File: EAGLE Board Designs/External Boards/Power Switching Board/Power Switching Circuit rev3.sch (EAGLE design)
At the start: 65 parts, among them J1 CONNECTOR-3_, J2 CONNECTOR-4_SOURIAU_, J3 CONNECTOR-4_SOURIAU_, Q1 TRANSISTOR_N_MOS_2-7K1S_TK100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, Q2 TRANSISTOR_N_MOS_2-7K1S_TK100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, Q3 TRANSISTOR_N_MOS_2-7K1S_TK100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, Q4 TRANSISTOR_N_MOS_2-7K1S_TK100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, U1 LTC4421

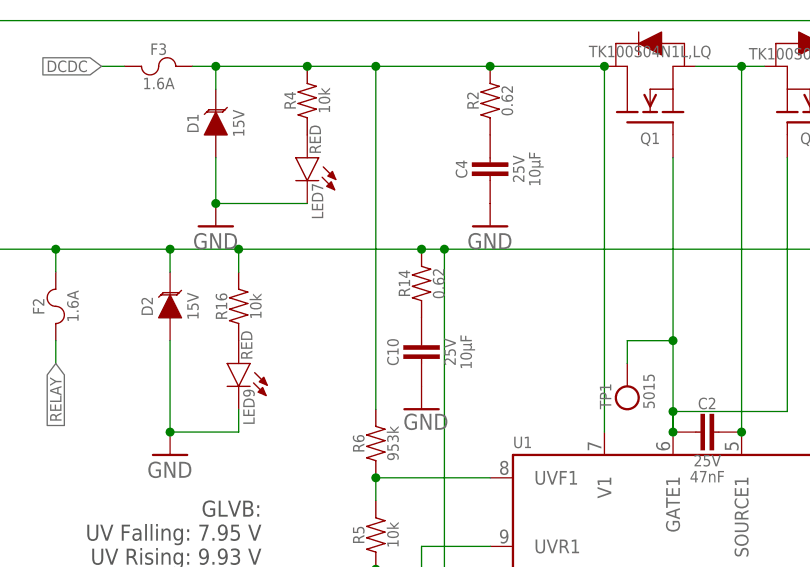
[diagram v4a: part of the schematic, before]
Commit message: Replaced 0.62 resistors with one in library
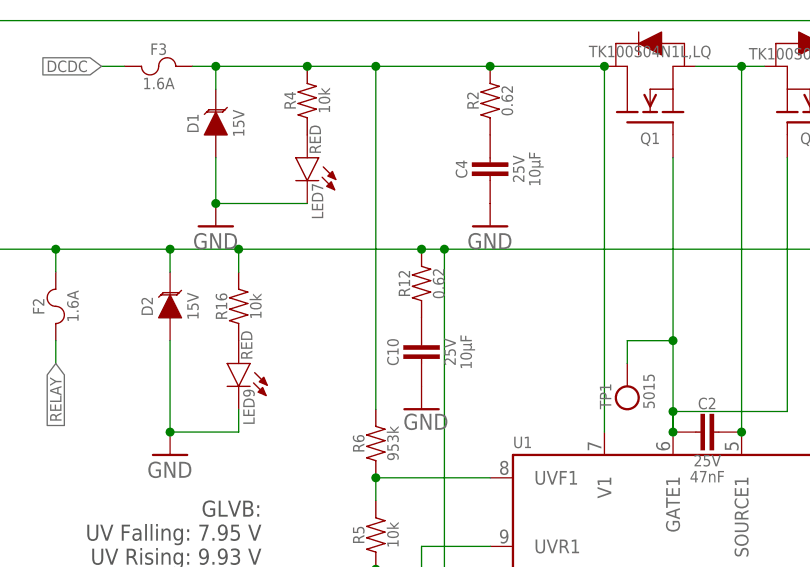
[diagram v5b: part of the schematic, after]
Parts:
- removed R14: 0.62, HyTechDevices:RESISTOR0805
- added R12: RESISTOR_0805_0.62, HyTechDevices:RESISTOR_0805_0.62
- R2: value 0.62 -> RESISTOR_0805_0.62; device HyTechDevices:RESISTOR0805 -> HyTechDevices:RESISTOR_0805_0.62
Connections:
- net N$4: now also R12.1; no longer R14.1
- net RELAY: now also R12.2; no longer R14.2
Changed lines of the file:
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@@
 <part name="GND10" library="HyTechSupplies" deviceset="GND" device=""/>
 <part name="GND11" library="HyTechSupplies" deviceset="GND" device=""/>
-<part name="R14" library="HyTechDevices" deviceset="RESISTOR" device="0805" value="0.62"/>
 <part name="GND12" library="HyTechSupplies" deviceset="GND" device=""/>
-<part name="R2" library="HyTechDevices" deviceset="RESISTOR" device="0805" value="0.62"/>
 <part name="GND13" library="HyTechSymbols" deviceset="GND" device=""/>
 <part name="D2" library="HyTechDevices" deviceset="TVS_*" device="" technology="15V"/>
@@
 <part name="GND15" library="HyTechSupplies" deviceset="GND" device=""/>
 <part name="C11" library="HyTechDevices" deviceset="CAPACITOR_?_*" device="0603" technology="25V_0.1UF"/>
+<part name="R2" library="HyTechDevices" deviceset="RESISTOR_?_*" device="0805" technology="0.62"/>
+<part name="R12" library="HyTechDevices" deviceset="RESISTOR_?_*" device="0805" technology="0.62"/>
 </parts>
 <sheets>
@@
 <attribute name="VALUE" x="-42.672" y="5.334" size="1.778" layer="96"/>
 </instance>
-<instance part="R14" gate="G$1" x="-40.64" y="22.86" smashed="yes" rot="R90">
-<attribute name="NAME" x="-41.91" y="21.59" size="1.27" layer="95" rot="R90" align="bottom-center"/>
-<attribute name="VALUE" x="-39.37" y="21.59" size="1.27" layer="96" rot="R90" align="top-center"/>
-</instance>
 <instance part="GND12" gate="1" x="-33.02" y="27.94" smashed="yes">
 <attribute name="VALUE" x="-35.56" y="25.4" size="1.778" layer="96"/>
-</instance>
-<instance part="R2" gate="G$1" x="-33.02" y="43.18" smashed="yes" rot="R90">
-<attribute name="NAME" x="-34.29" y="41.91" size="1.27" layer="95" rot="R90" align="bottom-center"/>
-<attribute name="VALUE" x="-31.75" y="41.91" size="1.27" layer="96" rot="R90" align="top-center"/>
 </instance>
 <instance part="GND13" gate="1" x="83.82" y="-30.48" smashed="yes">
@@
 <attribute name="VOLTAGE" x="40.64" y="87.63" size="1.27" layer="96" rot="R270" align="top-center"/>
 <attribute name="CAPACITANCE" x="38.862" y="87.63" size="1.27" layer="96" rot="R270" align="top-center"/>
+</instance>
+<instance part="R2" gate="G$1" x="-33.02" y="43.18" smashed="yes" rot="R90">
+<attribute name="NAME" x="-34.29" y="41.91" size="1.27" layer="95" rot="R90" align="bottom-center"/>
+<attribute name="RESISTANCE" x="-31.75" y="41.91" size="1.27" layer="96" rot="R90" align="top-center"/>
+</instance>
+<instance part="R12" gate="G$1" x="-40.64" y="22.86" smashed="yes" rot="R90">
+<attribute name="NAME" x="-41.91" y="21.59" size="1.27" layer="95" rot="R90" align="bottom-center"/>
+<attribute name="RESISTANCE" x="-39.37" y="21.59" size="1.27" layer="96" rot="R90" align="top-center"/>
 </instance>
 </instances>
@@
 <pinref part="U1" gate="G$1" pin="V1"/>
 <wire x1="-20.32" y1="5.08" x2="-20.32" y2="45.72" width="0.1524" layer="91"/>
+<junction x="-20.32" y="45.72"/>
+<pinref part="Q1" gate="G$1" pin="D"/>
 <wire x1="-20.32" y1="45.72" x2="-33.02" y2="45.72" width="0.1524" layer="91"/>
-<junction x="-20.32" y="45.72"/>
-<pinref part="R2" gate="G$1" pin="2"/>
-<pinref part="Q1" gate="G$1" pin="D"/>
+<pinref part="R4" gate="G$1" pin="2"/>
 <wire x1="-33.02" y1="45.72" x2="-45.72" y2="45.72" width="0.1524" layer="91"/>
-<junction x="-33.02" y="45.72"/>
-<pinref part="R4" gate="G$1" pin="2"/>
 <wire x1="-45.72" y1="45.72" x2="-53.34" y2="45.72" width="0.1524" layer="91"/>
 <wire x1="-53.34" y1="45.72" x2="-63.5" y2="45.72" width="0.1524" layer="91"/>
@@
 <junction x="-45.72" y="45.72"/>
 <pinref part="F3" gate="G$1" pin="2"/>
+<pinref part="R2" gate="G$1" pin="2"/>
+<junction x="-33.02" y="45.72"/>
 </segment>
 <segment>
@@
 <net name="RELAY" class="0">
 <segment>
-<pinref part="R14" gate="G$1" pin="2"/>
 <pinref part="R16" gate="G$1" pin="2"/>
 <wire x1="-81.28" y1="25.4" x2="-68.58" y2="25.4" width="0.1524" layer="91"/>
 <wire x1="-68.58" y1="25.4" x2="-60.96" y2="25.4" width="0.1524" layer="91"/>
 <wire x1="-60.96" y1="25.4" x2="-40.64" y2="25.4" width="0.1524" layer="91"/>
+<wire x1="-40.64" y1="25.4" x2="-38.1" y2="25.4" width="0.1524" layer="91"/>
 <wire x1="-60.96" y1="22.86" x2="-60.96" y2="25.4" width="0.1524" layer="91"/>
 <junction x="-60.96" y="25.4"/>
@@
 <pinref part="U1" gate="G$1" pin="V2"/>
 <wire x1="5.08" y1="5.08" x2="5.08" y2="25.4" width="0.1524" layer="91"/>
-<wire x1="-40.64" y1="25.4" x2="-38.1" y2="25.4" width="0.1524" layer="91"/>
-<junction x="-40.64" y="25.4"/>
 <junction x="5.08" y="25.4"/>
 <pinref part="R8" gate="G$1" pin="2"/>
@@
 <pinref part="U$10" gate="G$1" pin="CONTACT2"/>
 <wire x1="-81.28" y1="25.4" x2="-91.44" y2="25.4" width="0.1524" layer="91"/>
+<pinref part="R12" gate="G$1" pin="2"/>
+<junction x="-40.64" y="25.4"/>
 </segment>
 <segment>
@@
 </segment>
 </net>
-<net name="N$22" class="0">
-<segment>
-<pinref part="R2" gate="G$1" pin="1"/>
-<pinref part="C4" gate="G$1" pin="1"/>
-</segment>
-</net>
-<net name="N$4" class="0">
-<segment>
-<pinref part="R14" gate="G$1" pin="1"/>
-<pinref part="C10" gate="G$1" pin="1"/>
-</segment>
-</net>
 <net name="N$2" class="0">
 <segment>
@@
 </segment>
 </net>
+<net name="N$22" class="0">
+<segment>
+<pinref part="C4" gate="G$1" pin="1"/>
+<pinref part="R2" gate="G$1" pin="1"/>
+</segment>
+</net>
+<net name="N$4" class="0">
+<segment>
+<pinref part="C10" gate="G$1" pin="1"/>
+<pinref part="R12" gate="G$1" pin="1"/>
+</segment>
+</net>

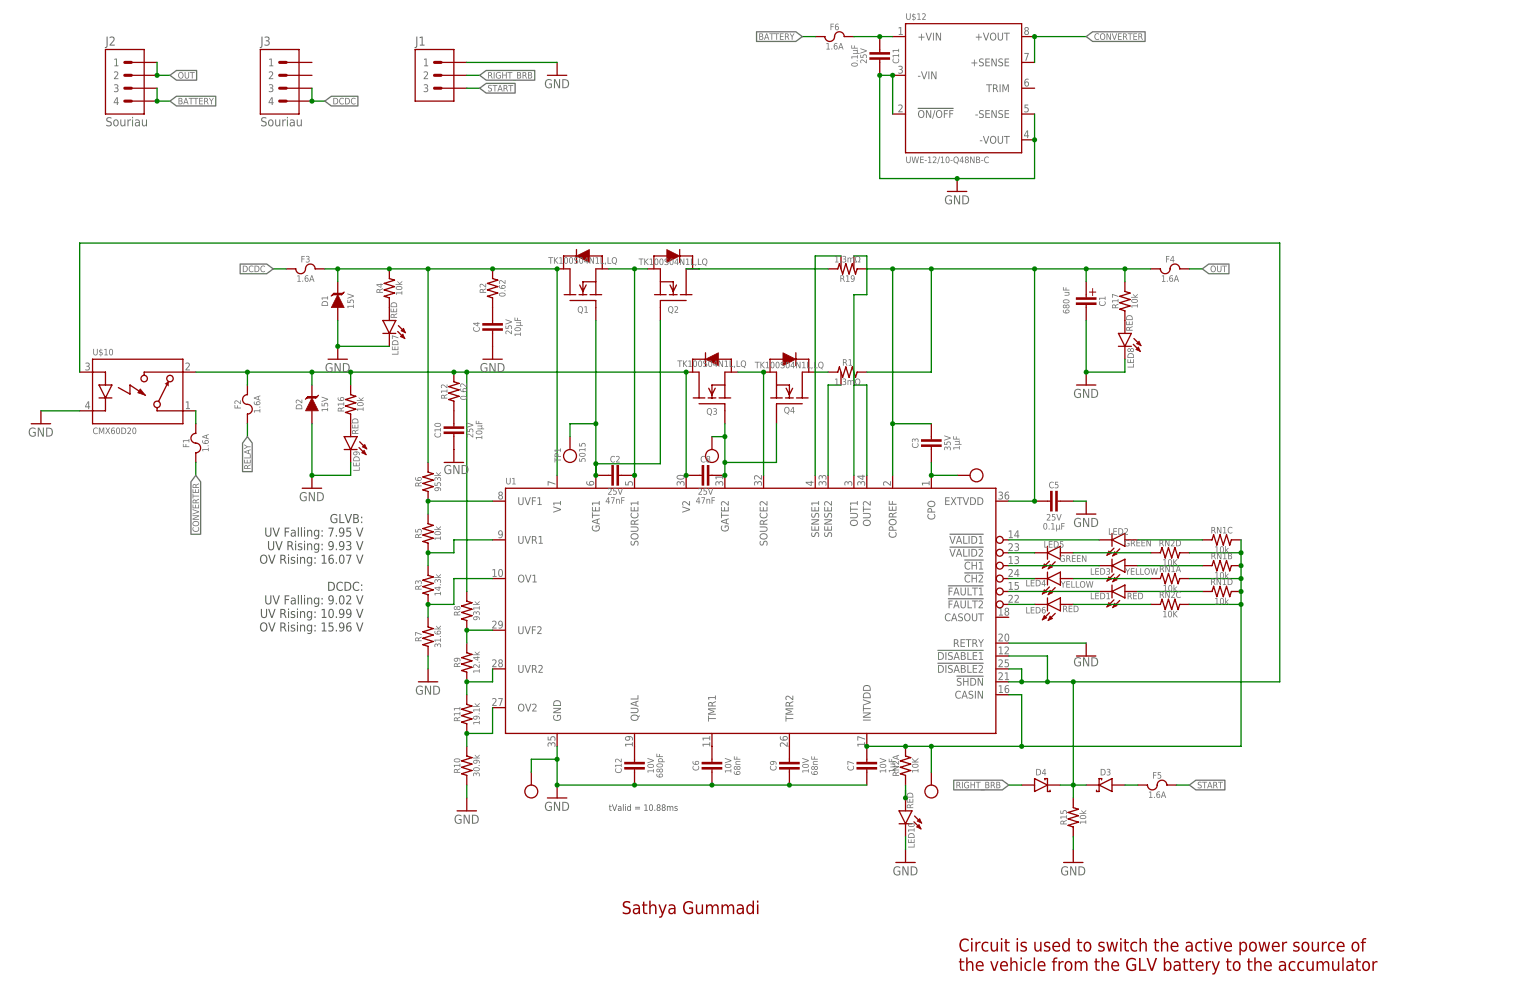
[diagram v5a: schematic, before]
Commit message: Replaced fuses with 10A blade fuses
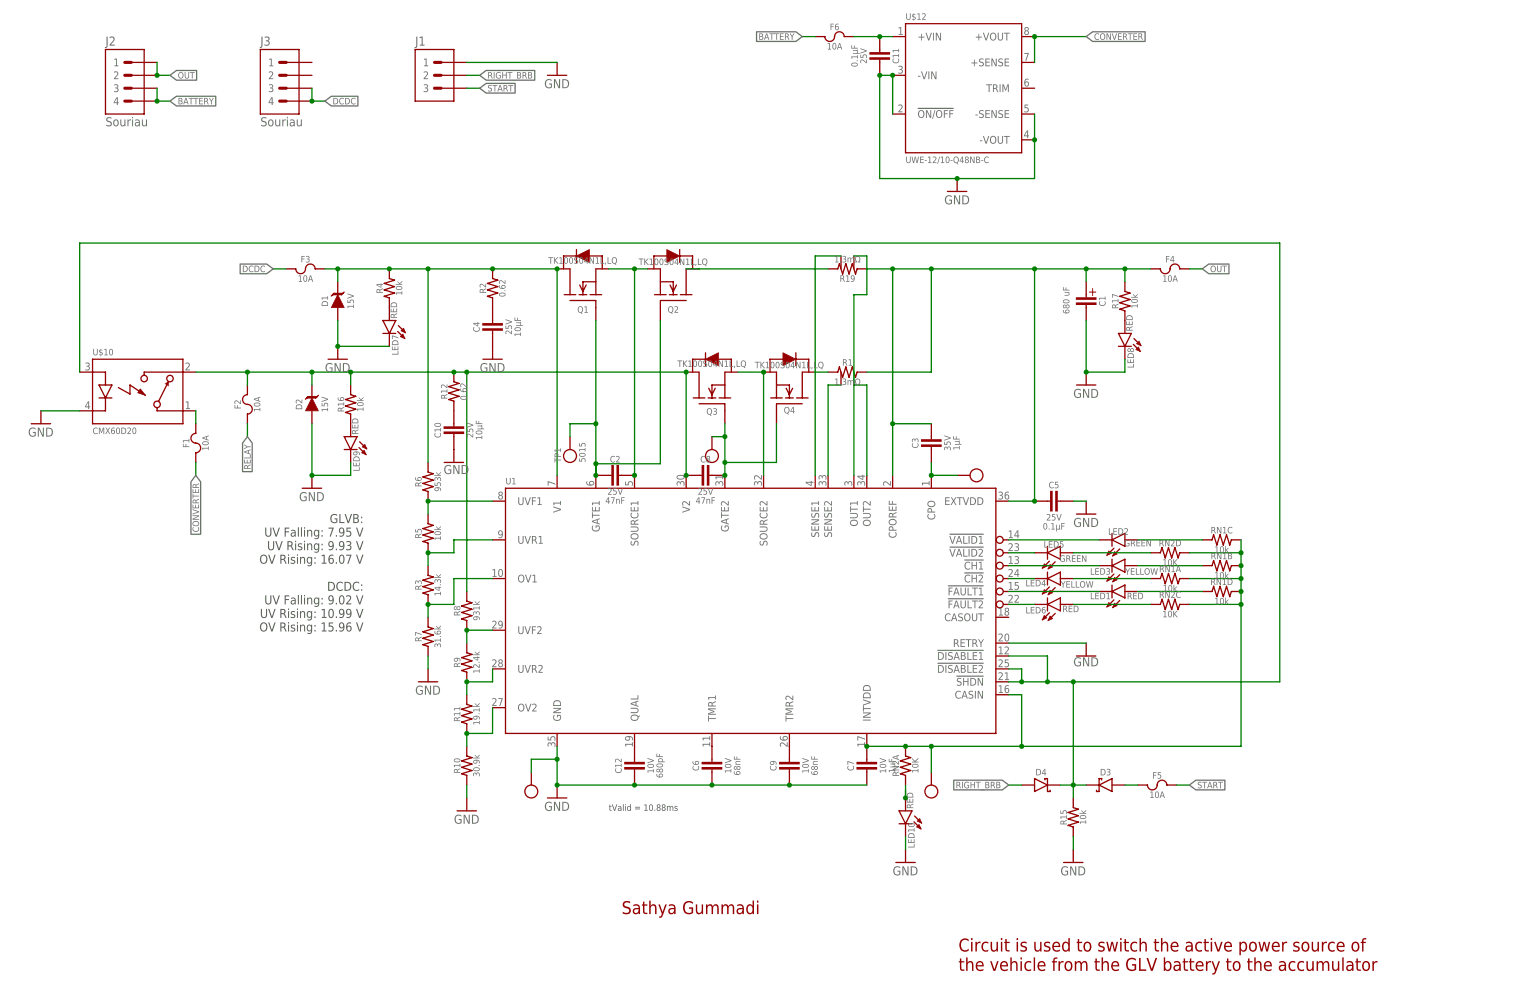
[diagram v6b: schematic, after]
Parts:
- F1, F2, F3, F4, F5, F6: value FUSE_0885_1.6 -> FUSE_MB_10; device HyTechDevices:FUSE_0885_1.6 -> HyTechDevices:FUSE_MB_10
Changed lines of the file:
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@@
 <part name="RN2" library="HyTechDevices" deviceset="RESISTOR_NETWORK_4_*" device="" technology="10K"/>
 <part name="U$11" library="HyTechDevices" deviceset="TEST_POINT" device=""/>
-<part name="F1" library="HyTechDevices" deviceset="FUSE_?_*" device="0885" technology="1.6"/>
-<part name="F2" library="HyTechDevices" deviceset="FUSE_?_*" device="0885" technology="1.6"/>
-<part name="F3" library="HyTechDevices" deviceset="FUSE_?_*" device="0885" technology="1.6"/>
-<part name="F4" library="HyTechDevices" deviceset="FUSE_?_*" device="0885" technology="1.6"/>
+<part name="F1" library="HyTechDevices" deviceset="FUSE_?_*" device="MB" technology="10" value="FUSE_MB_10"/>
+<part name="F2" library="HyTechDevices" deviceset="FUSE_?_*" device="MB" technology="10" value="FUSE_MB_10"/>
+<part name="F3" library="HyTechDevices" deviceset="FUSE_?_*" device="MB" technology="10" value="FUSE_MB_10"/>
+<part name="F4" library="HyTechDevices" deviceset="FUSE_?_*" device="MB" technology="10" value="FUSE_MB_10"/>
 <part name="C12" library="HyTechDevices" deviceset="CAPACITOR_?_*" device="0603" technology="10V_680PF"/>
 <part name="C7" library="HyTechDevices" deviceset="CAPACITOR_?_*" device="0603" technology="10V_1UF"/>
@@
 <part name="C3" library="HyTechDevices" deviceset="CAPACITOR_?_*" device="0603" technology="35V_1UF"/>
 <part name="C4" library="HyTechDevices" deviceset="CAPACITOR_?_*" device="0603" technology="25V_10UF"/>
-<part name="F5" library="HyTechDevices" deviceset="FUSE_?_*" device="0885" technology="1.6"/>
+<part name="F5" library="HyTechDevices" deviceset="FUSE_?_*" device="MB" technology="10" value="FUSE_MB_10"/>
 <part name="C2" library="HyTechDevices" deviceset="CAPACITOR_?_*" device="0603" technology="25V_47NF"/>
 <part name="C8" library="HyTechDevices" deviceset="CAPACITOR_?_*" device="0603" technology="25V_47NF"/>
@@
 <part name="U$10" library="HyTechDevices" deviceset="RELAY_SOLIDSTATE_NO_?*" device="" technology="CMX60D20"/>
 <part name="U$12" library="HyTechDevices" deviceset="UWE-*" device="" technology="12/10-Q48NB-C"/>
-<part name="F6" library="HyTechDevices" deviceset="FUSE_?_*" device="0885" technology="1.6"/>
+<part name="F6" library="HyTechDevices" deviceset="FUSE_?_*" device="MB" technology="10" value="FUSE_MB_10"/>
 <part name="GND15" library="HyTechSupplies" deviceset="GND" device=""/>
 <part name="C11" library="HyTechDevices" deviceset="CAPACITOR_?_*" device="0603" technology="25V_0.1UF"/>
